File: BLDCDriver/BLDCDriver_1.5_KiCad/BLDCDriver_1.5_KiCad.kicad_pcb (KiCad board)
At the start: 2 copper layers, 27.9 x 35.6 mm, 41 parts, among them IC1 STSPIN32G4, J1 Conn_01x02_Male, U4 MCP2562-E-SN, U5 AS5048A-HTSP-500, Y1 12Mhz

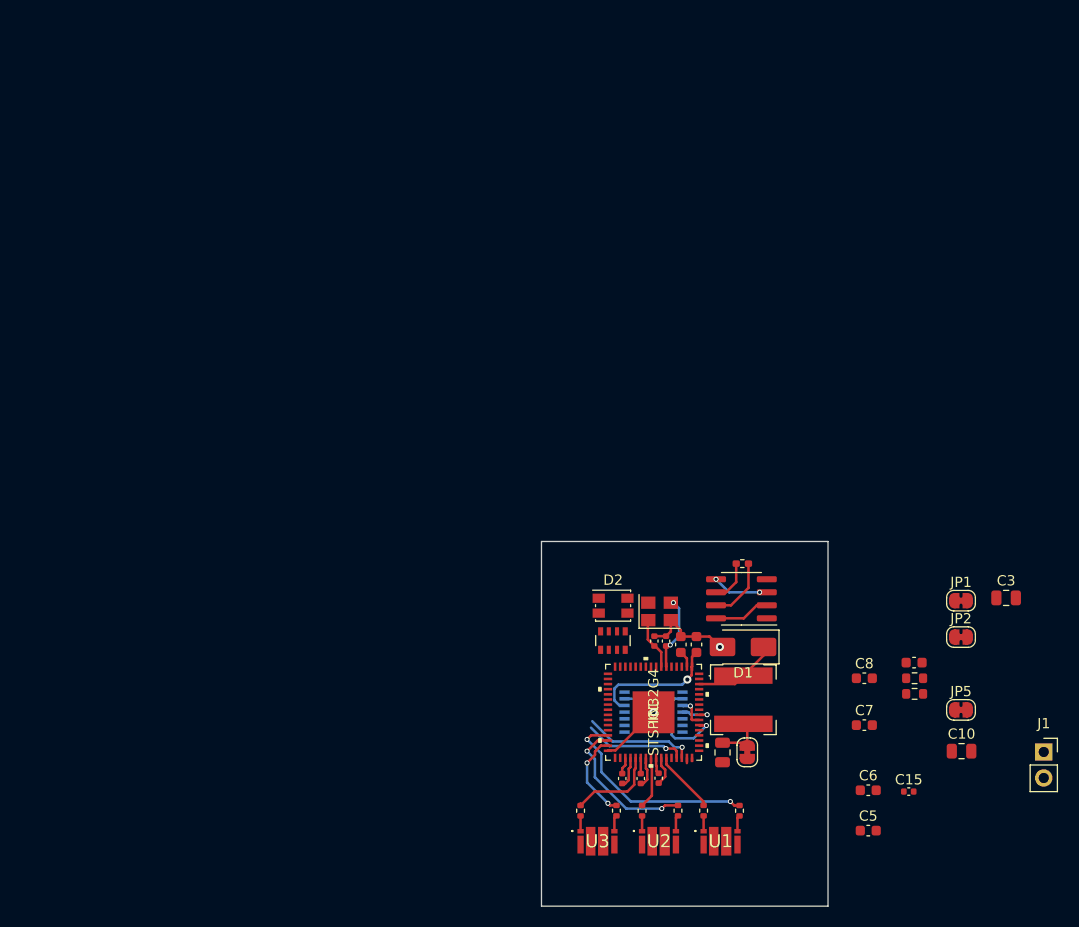
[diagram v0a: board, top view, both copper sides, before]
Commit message: ✨基板外形の更新と3Dデータのインポートをした
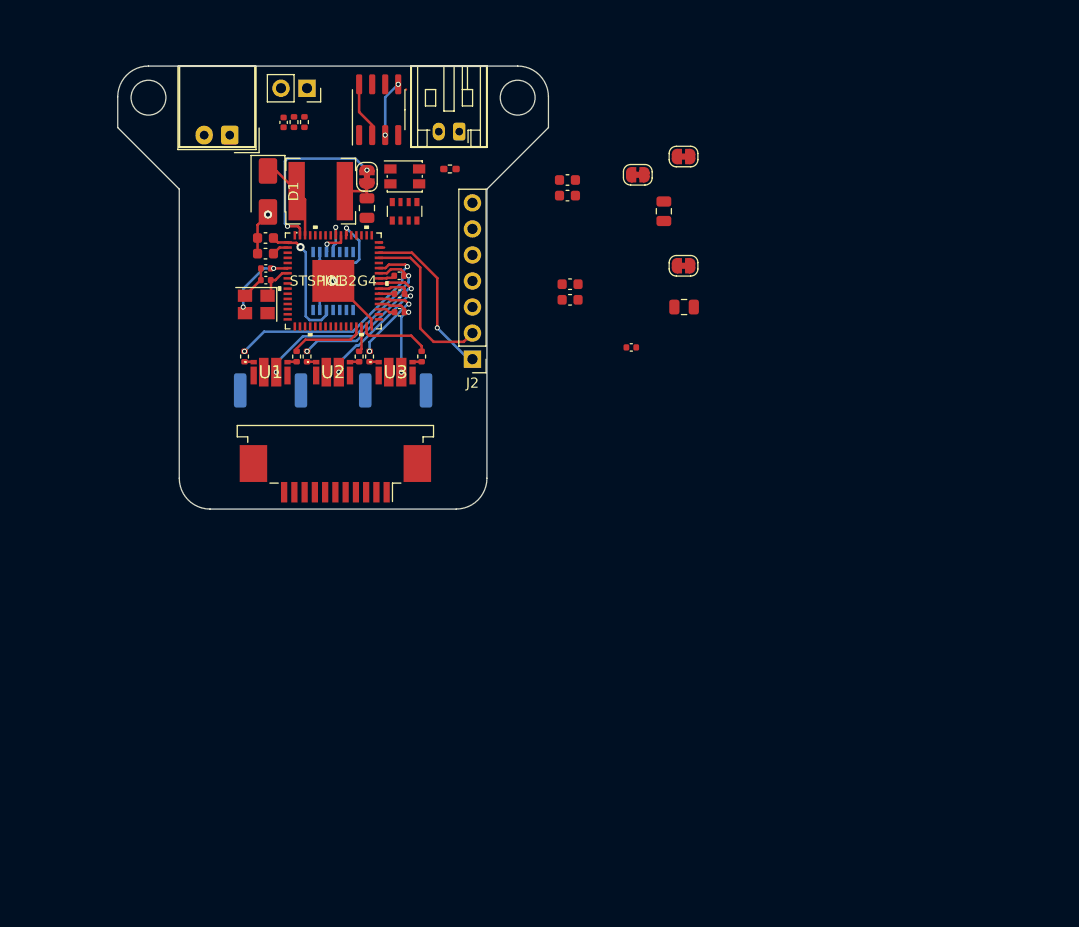
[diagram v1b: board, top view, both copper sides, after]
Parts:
- added J2: Conn_01x07_Pin, Connector_PinHeader_2.54mm:PinHeader_1x07_P2.54mm_Vertical, F.Cu at (13.6, 7.62)
- added J3: Motor Out, Connector_FFC-FPC:TE_1-84952-1_1x11-1MP_P1.0mm_Horizontal, F.Cu at (0.22, 18.8)
- added J4: POWER, Connector_Molex:Molex_SPOX_5268-02A_1x02_P2.50mm_Horizontal, F.Cu at (-10.1, -14.2)
- added J5: CAN, Connector_JST:JST_PH_S2B-PH-K_1x02_P2.00mm_Horizontal, F.Cu at (12.3, -14.6)
- added R10: 4mΩ, Resistor_SMD:R_2512_6332Metric, B.Cu at (-6.10, 10.7)
- added R11: 4mΩ, Resistor_SMD:R_2512_6332Metric, B.Cu at (6.10, 10.7)
- C12: footprint Capacitor_SMD:C_0603_1608Metric -> Capacitor_SMD:C_0402_1005Metric
- R1, R2: footprint Resistor_SMD:R_0603_1608Metric -> Resistor_SMD:R_0402_1005Metric
- R4, R5, R6, R7, R8, R9: value 22k -> 51
- moved J1 96.7 mm to (-2.54, -18.8), turned to -90 degrees
- moved R2 81.5 mm to (-2.79, -15.5), turned to 90 degrees
- moved R1 81.3 mm to (-3.81, -15.5), turned to 90 degrees
- moved C12 81.0 mm to (-4.83, -15.5), turned to -90 degrees
- moved JP3 67.3 mm to (3.30, -10.2), turned to 90 degrees
- moved L1 64.5 mm to (-1.21, -8.76), turned to 0 degrees
- moved D1 64.2 mm to (-6.35, -8.73), turned to -90 degrees
- moved C$1 63.4 mm to (3.30, -7.11)
- moved U1 63.4 mm to (-6.10, 8.89)
- moved R4 63.0 mm to (-8.64, 7.36)
- moved R5 61.9 mm to (-3.56, 7.36)
- moved U4 59.4 mm to (4.45, -16.7), turned to 90 degrees
- moved C5 59.4 mm to (23.1, 1.83)
- moved C7 59.2 mm to (22.9, -8.32)
- moved C4 57.8 mm to (-6.59, -4.19), turned to 180 degrees
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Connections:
- IC1 pad 10: VOUT2 -> unconnected-(IC1-PC1-Pad10)
- IC1 pad 11: VOUT3 -> unconnected-(IC1-PC2-Pad11)
- IC1 pad 13: VBUS -> unconnected-(IC1-PA0-Pad13)
- IC1 pad 28: USER2 -> SW
- IC1 pad 9: VOUT1 -> unconnected-(IC1-PC0-Pad9)
- U1 pad 5: GND -> Net-(U1-S)
- U3 pad 5: GND -> Net-(U3-S)
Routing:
- net OUT1: track 2.89 -> 21.2 mm, vias 0 -> 2
- net VCC: track 0.00 -> 17.0 mm, vias 0 -> 2
- net GHS1: track 6.14 -> 22.9 mm, vias 0 -> 2
- net GLS1: track 20.8 -> 7.40 mm, vias 2 -> 0
- net GLS2: track 14.8 -> 2.51 mm, vias 2 -> 0
- net OUT2: track 2.96 -> 14.6 mm, vias 0 -> 2
- net GHS2: track 5.08 -> 16.1 mm, vias 0 -> 2
- net OUT3: track 3.01 -> 9.70 mm, vias 0 -> 2
- net UART_TX: track 9.97 -> 16.3 mm, vias 1 -> 0
- net CANH: track 6.23 -> 0.00 mm
- net UART_RX: track 10.9 -> 16.3 mm
- net CANL: track 4.18 -> 0.00 mm
- net GND: track 24.7 -> 23.1 mm
- net GLS3: track 8.63 -> 7.05 mm, vias 2 -> 0
- net Net-(IC1-PF1): track 5.14 -> 3.61 mm
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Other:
- board size 27.9 x 35.6 mm -> 42 x 43.2 mm

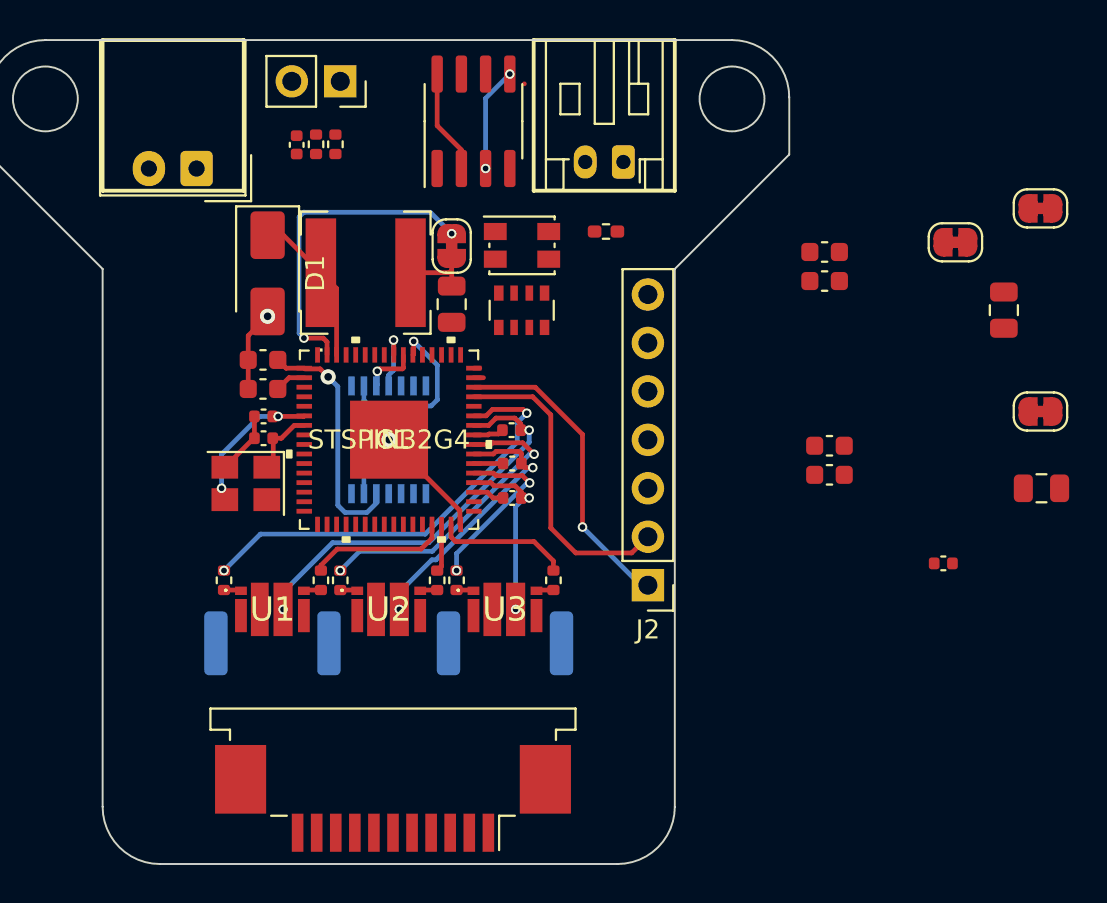
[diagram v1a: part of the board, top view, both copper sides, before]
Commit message: ✨回路を進めたよ。あとアートワーク太くするだけ。
CANの電源が3.3Vだと厳しい印象。
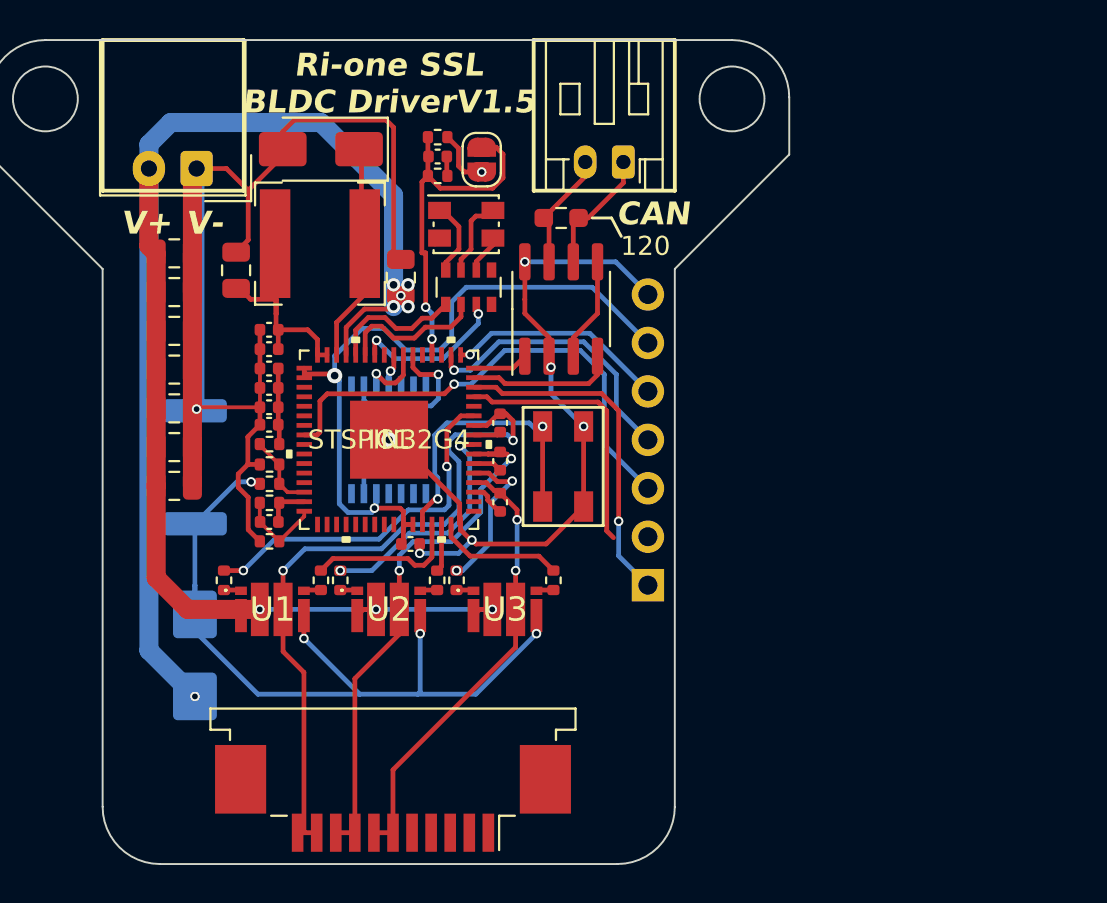
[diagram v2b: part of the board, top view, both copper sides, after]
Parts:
- removed J1: Conn_01x02_Male, Connector_PinSocket_2.54mm:PinSocket_1x02_P2.54mm_Vertical
- removed JP2, JP3, JP5: Jumper_2_Bridged, Jumper:SolderJumper-2_P1.3mm_Bridged_RoundedPad1.0x1.5mm
- removed R11: 4mΩ, Resistor_SMD:R_2512_6332Metric
- removed Y1: 12Mhz, Crystal:Crystal_SMD_3225-4Pin_3.2x2.5mm
- added C16: 1uF, Capacitor_SMD:C_0402_1005Metric, F.Cu at (-6.26, 4.30)
- added C17: 22uF, Capacitor_SMD:C_0805_2012Metric, F.Cu at (-11.2, -3.68)
- added C18: 22uF, Capacitor_SMD:C_0805_2012Metric, F.Cu at (-11.2, -5.71)
- added C19: 22uF, Capacitor_SMD:C_0805_2012Metric, F.Cu at (-11.2, -7.75)
- added C20: 22uF, Capacitor_SMD:C_0805_2012Metric, F.Cu at (-11.2, -9.78)
- added R12: 1.5k, Resistor_SMD:R_0402_1005Metric, F.Cu at (-6.25, 2.31)
- added R13: 1.5k, Resistor_SMD:R_0402_1005Metric, F.Cu at (-6.25, 5.32)
- added R14: 22k, Resistor_SMD:R_0402_1005Metric, F.Cu at (-6.25, 0.22)
- added R15: 22k, Resistor_SMD:R_0402_1005Metric, F.Cu at (-6.25, 1.29)
- added R16: 1.5k, Resistor_SMD:R_0402_1005Metric, F.Cu at (-6.25, 3.30)
- added SW1: SW_Push, newinov-kicad:SKRPACE010, F.Cu at (9.14, 1.40)
- added TVS1: 16V, Diode_SMD:D_SMB, B.Cu at (-10.2, 11.3)
- C1, C2: value 20p -> 22uF; footprint Capacitor_SMD:C_0402_1005Metric -> Capacitor_SMD:C_0805_2012Metric
- C3: footprint Capacitor_SMD:C_0805_2012Metric -> Capacitor_SMD:C_0402_1005Metric
- C4, C6, C8: footprint Capacitor_SMD:C_0603_1608Metric -> Capacitor_SMD:C_0402_1005Metric
- C5, C7: value 1uF -> 10uF; footprint Capacitor_SMD:C_0603_1608Metric -> Capacitor_SMD:C_0402_1005Metric
- C9: value 100nF -> 22uF; footprint Capacitor_SMD:C_0603_1608Metric -> Capacitor_SMD:C_0805_2012Metric
- J2: value Conn_01x07_Pin -> Debug; moved to B.Cu
- JP1: value Jumper_2_Bridged -> Jumper_2_Open; footprint Jumper:SolderJumper-2_P1.3mm_Bridged_RoundedPad1.0x1.5mm -> Jumper:SolderJumper-2_P1.3mm_Open_RoundedPad1.0x1.5mm
- R3: footprint Resistor_SMD:R_0402_1005Metric_Pad0.72x0.64mm_HandSolder -> Resistor_SMD:R_0603_1608Metric_Pad0.98x0.95mm_HandSolder
- moved C3 39.0 mm to (-6.27, -0.79), turned to 180 degrees
- moved C10 35.4 mm to (0.64, -8.51), turned to -90 degrees
- moved C5 29.6 mm to (-6.27, -1.71), turned to 180 degrees
- moved C8 29.6 mm to (-6.27, -4.75), turned to 180 degrees
- moved C6 29.5 mm to (-6.27, -2.72), turned to 180 degrees
- moved JP1 29.4 mm to (4.88, -14.7), turned to -90 degrees
- moved C7 29.2 mm to (-6.27, -5.77), turned to 180 degrees
- moved C15 28.0 mm to (1.14, 5.46), turned to 180 degrees
- moved C$1 11.4 mm to (-8.00, -8.89), turned to 90 degrees
- moved U4 10.9 mm to (9.04, -6.86)
- moved R10 10.1 mm to (-10.2, 1.44), turned to -90 degrees
- moved C12 7.42 mm to (2.57, -14.9), turned to 0 degrees
- moved D1 7.08 mm to (-3.56, -15.2), turned to 180 degrees
- moved R1 6.39 mm to (2.57, -15.9), turned to 180 degrees
- moved C1 5.93 mm to (-11.2, 2.41)
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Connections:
- C$1 pad 1: Net-(JP3-A) -> VCC
- C1 pad 1: Net-(IC1-PF0) -> GND
- C1 pad 2: GND -> VD
- C10 pad 1: Net-(IC1-VM) -> GND
- C10 pad 2: GND -> VD
- C2 pad 1: Net-(IC1-PF1) -> GND
- C2 pad 2: GND -> VD
- C5 pad 1: VDDA -> VDD
- C6 pad 1: VDDA -> VDD
- C7 pad 1: VREF+ -> VCC
- C8 pad 1: VREF+ -> VCC
- C9 pad 1: VBAT -> GND
- C9 pad 2: GND -> VD
- D1 pad 1: SW -> GVCC_SW
- IC1 pad 14: unconnected-(IC1-PA1-Pad14) -> OP_+1
- IC1 pad 15: unconnected-(IC1-PA2-Pad15) -> OP_O1
- IC1 pad 16: unconnected-(IC1-PA3-Pad16) -> OP_-1
- IC1 pad 18: DAC2 -> unconnected-(IC1-PA5-Pad18)
- IC1 pad 2: VBAT -> VDD
- IC1 pad 26: VREF+ -> VDD
- IC1 pad 27: VDDA -> VDD
- IC1 pad 3: USER1 -> unconnected-(IC1-PC13-Pad3)
- IC1 pad 58: unconnected-(IC1-PB7-Pad58) -> LED_B
- IC1 pad 59: unconnected-(IC1-PB8-Pad59) -> LED_G
- IC1 pad 6: Net-(IC1-PF0) -> unconnected-(IC1-PF0-Pad6)
- IC1 pad 60: unconnected-(IC1-PB9-Pad60) -> LED_R
- IC1 pad 61: Net-(IC1-VM) -> VD
- IC1 pad 62: SW -> GVCC_SW
- IC1 pad 64: VREGIN -> VCC
- IC1 pad 7: Net-(IC1-PF1) -> unconnected-(IC1-PF1-Pad7)
- J3 pad MP: GND -> unconnected-(J3-MountPin-PadMP)
- J4 pad 1: VD -> GND
- J4 pad 2: GND -> VD
- J5 pad 1: CANH -> CANL
- J5 pad 2: CANL -> CANH
- JP1 pad 1: VCC -> SCREF
- JP1 pad 2: VREGIN -> VDD
- L1 pad 1: SW -> GVCC_SW
- L1 pad 2: Net-(JP3-A) -> VCC
- R10 pad 2: Net-(U1-S) -> SHUNT_P1
- U1 pad 5: Net-(U1-S) -> SHUNT_P1
- U2 pad 5: GND -> SHUNT_P1
- U3 pad 5: Net-(U3-S) -> SHUNT_P1
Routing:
- net VD: track 0.00 -> 99.0 mm, vias 0 -> 9
- net GND: track 23.1 -> 115.6 mm, vias 2 -> 7
- net SHUNT_P1: track 0.00 -> 42.6 mm, vias 0 -> 4
- net VDD: track 18.3 -> 51.0 mm
- net nRST: track 0.00 -> 26.0 mm, vias 0 -> 1
- net SCREF: track 0.00 -> 18.9 mm, vias 0 -> 2
- net OUT1: track 21.2 -> 36.7 mm
- net SWCLK: track 0.00 -> 14.8 mm, vias 0 -> 1
- net OUT3: track 9.70 -> 23.5 mm
- net OUT2: track 14.6 -> 27.9 mm
- net SWDIO: track 0.00 -> 11.6 mm, vias 0 -> 1
- net GVCC_SW: track 0.00 -> 11.5 mm
- net LED_B: track 0.00 -> 8.35 mm, vias 0 -> 2
- net Net-(IC1-PF0): track 8.18 -> 0.00 mm, vias 2 -> 0
- net LED_G: track 0.00 -> 7.70 mm
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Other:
- board text added: "3.3V"
- board text added: "CAN"
- board text added: "GND"
- board text added: "RST"
- board text added: "RX"
- board text added: "Ri-one SSL BLDC DriverV1.5"
- board text added: "SWC"
- board text added: "SWD"
- board text added: "TX"
- board text added: "V+"
- board text added: "V-"

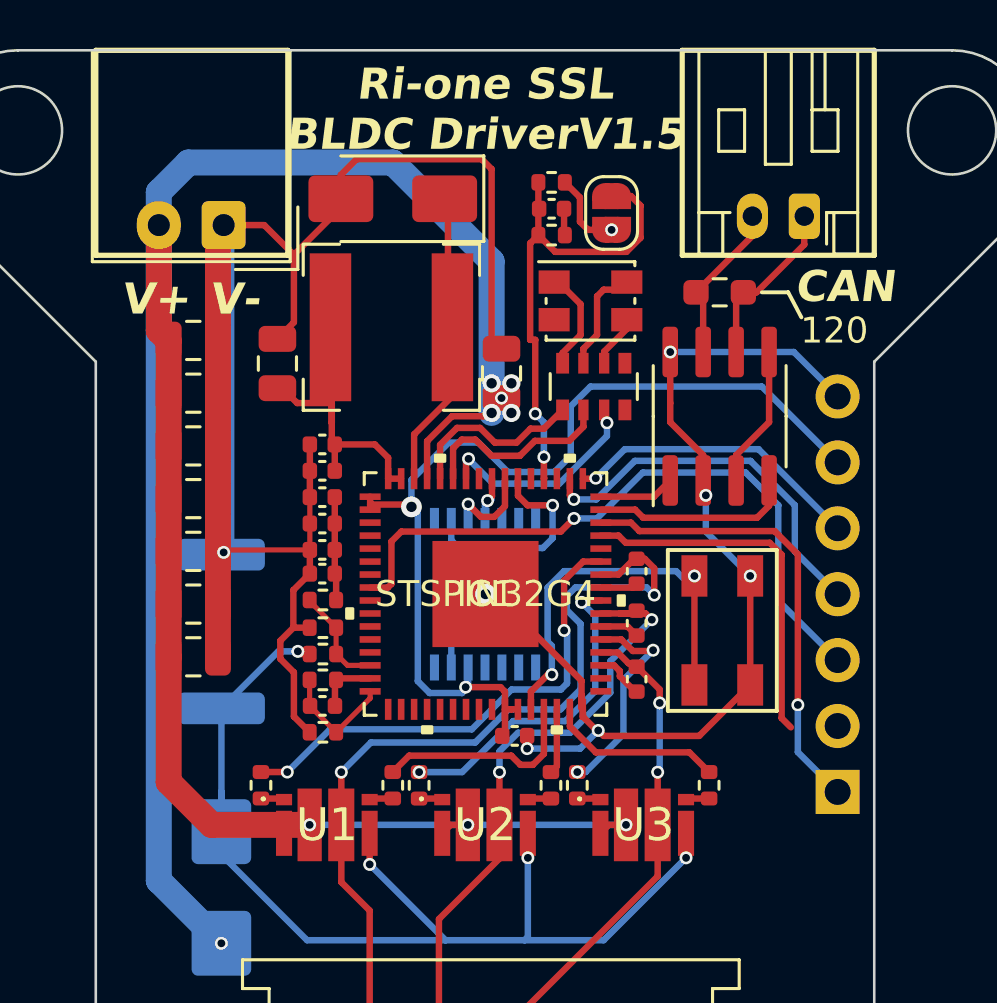
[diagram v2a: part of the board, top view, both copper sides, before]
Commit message: ✨DRCエラーを修正した
MOSFETとゲート抵抗が近すぎると表示されるやつに関しては無視で行くしかない。
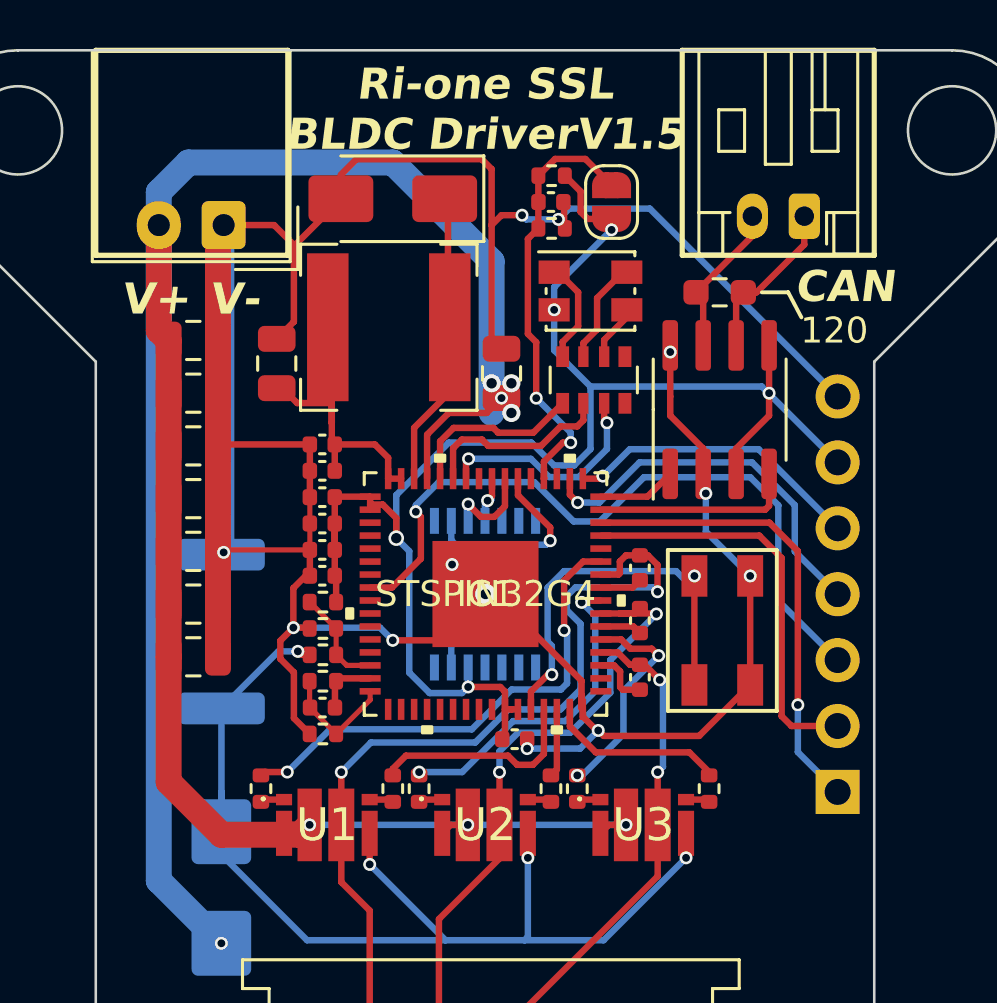
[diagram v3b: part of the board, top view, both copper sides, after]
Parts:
- moved JP1 0.42 mm to (4.88, -15.1)
- moved D2 0.38 mm to (4.06, -11.7)
- moved C12 0.26 mm to (2.54, -15.1)
- moved R1 0.26 mm to (2.57, -16.1)
- moved R2 0.26 mm to (2.57, -14.1)
- moved RN1 0.25 mm to (4.19, -8.26)
- moved U4 0.25 mm to (9.04, -7.11)
- moved C11 0.18 mm to (5.97, -1.02)
- moved C13 0.16 mm to (5.97, 1.02)
- moved C14 0.15 mm to (5.97, 3.20)
- moved R4 0.13 mm to (-8.64, 7.49)
- moved R5 0.13 mm to (-3.56, 7.49)
- moved R8 0.13 mm to (3.56, 7.49)
- moved R9 0.13 mm to (8.64, 7.49)
- moved R6 0.13 mm to (-2.54, 7.49)
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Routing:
- net GND: track 115.6 -> 139.6 mm, vias 7 -> 12
- net VDD: track 51.0 -> 62.0 mm, vias 3 -> 5
- net SCREF: track 18.9 -> 17.2 mm
- net UART_TX: track 14.1 -> 15.8 mm
- net nRST: track 26.0 -> 27.6 mm
- net SPI1_SCK: track 8.35 -> 7.60 mm
- net OUT2: track 27.9 -> 28.5 mm
- net OUT1: track 36.7 -> 37.2 mm
- net VD: track 99.0 -> 99.4 mm, vias 9 -> 8
